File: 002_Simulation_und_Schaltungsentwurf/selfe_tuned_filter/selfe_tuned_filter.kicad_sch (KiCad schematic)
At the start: 37 parts, among them IC1 MPY634KP, IC2 MPY634KP, IC3 MPY634KP, J1 Screw_Terminal_01x04, U1 TL082, U2 TL082, U3 TL082

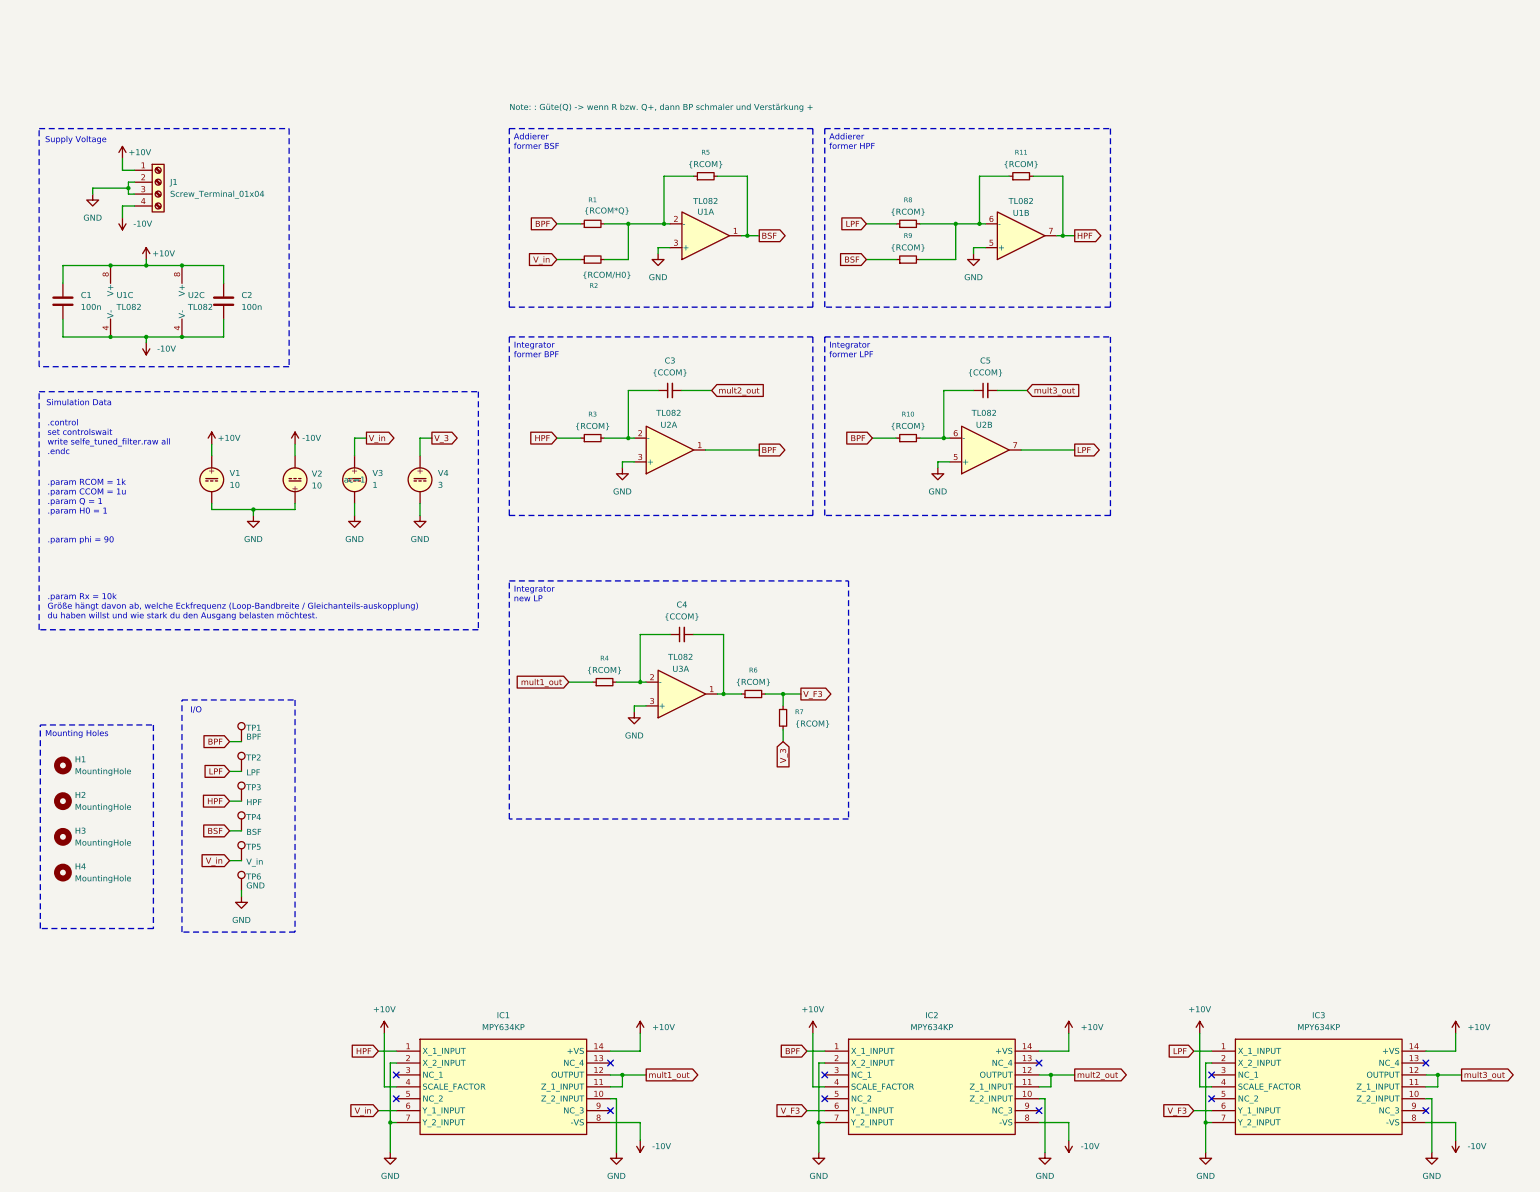
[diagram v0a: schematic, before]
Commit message: Simulation muss aufgrund von neuistallation von KiCad neu gemaucht werden, 1/2 fertig
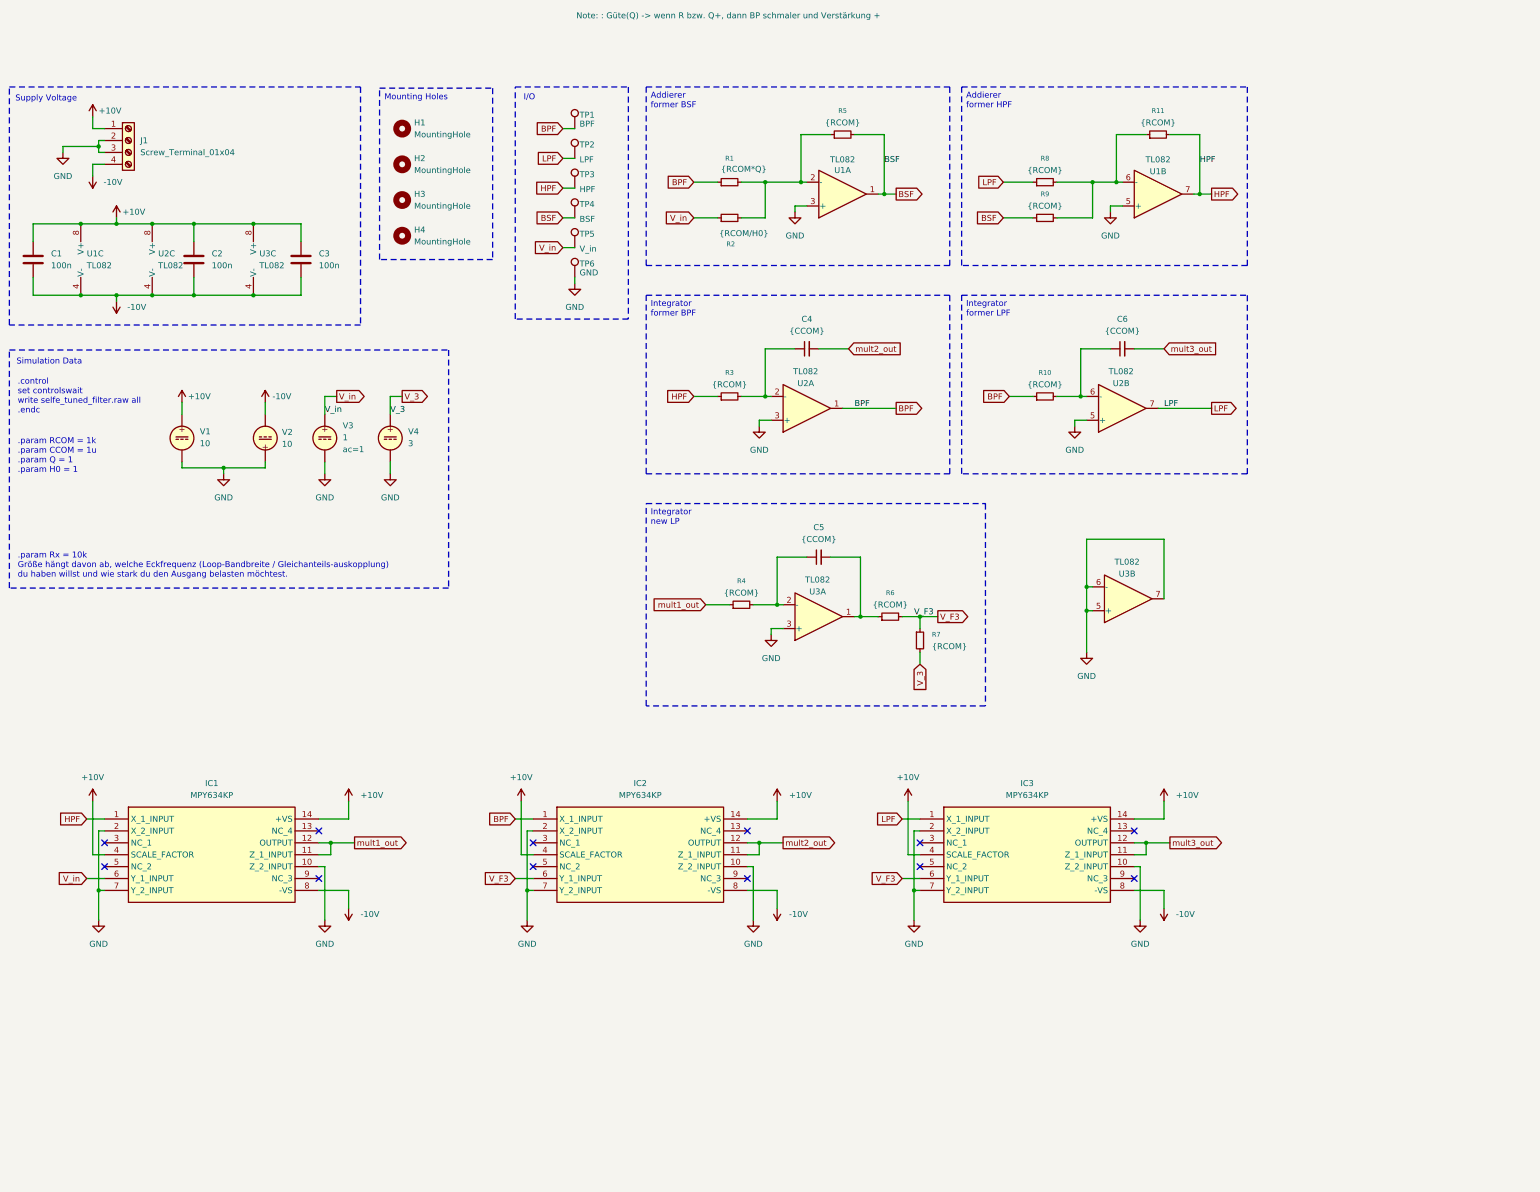
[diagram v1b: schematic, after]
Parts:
- added C3: 100n, Capacitor_THT:C_Disc_D3.0mm_W2.0mm_P2.50mm, symbol Device:C
- added unit 2 of U3
- added unit 3 of U3
- IC1, IC2, IC3: footprint DIP794W53P254L1930H508Q14N -> (none)
- R1, R2: footprint 000_Footprints:Trimmer straight -> 000_Footprints:Resistor
- renumbered C3 to C4, C4 to C5, C5 to C6
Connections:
- net +10V: now also C3.1, U3.8 (V+)
- net -10V: now also C3.2, U3.4 (V-)
- net GND: now also U3.5 (+), U3.6 (-), U3.7
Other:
- note added: ".param RCOM = 1k .param CCOM = 1u .param Q = 1 .param H0 = 1"
- note removed: ".param RCOM = 1k .param CCOM = 1u .param Q = 1 .param H0 = 1 .param phi = 90"
- moved on the sheet: C1, C2, C4, C5, C6, H1, H2, H3, H4, IC1, IC2, IC3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

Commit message: chore:add untracked files
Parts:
- removed R2: {RCOM/H0}, 000_Footprints:Resistor, symbol Device:R_Small
- removed unit 2 of U3
- added R12: {RCOM*Q}, 000_Footprints:Resistor, symbol Device:R_Small
- R1: value {RCOM*Q} -> {RCOM/H0}; Note:  Güte(Q) -> wenn R bzw. Q+, dann BP schmaler und Verstärkung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 -> (none)
- V1, V2: value 10 -> 15
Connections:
- net BPF: now also R12.1; no longer R1.1
- net V_in: now also R1.1
- net at R1.2, R5.1, U1.2 (-): now also R12.2
- net V_3 renamed +3V
